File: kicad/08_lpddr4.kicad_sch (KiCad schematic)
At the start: 42 parts, among them U501 Ti135N484I3, U801 H9HCNNN8KUMLHR-NME

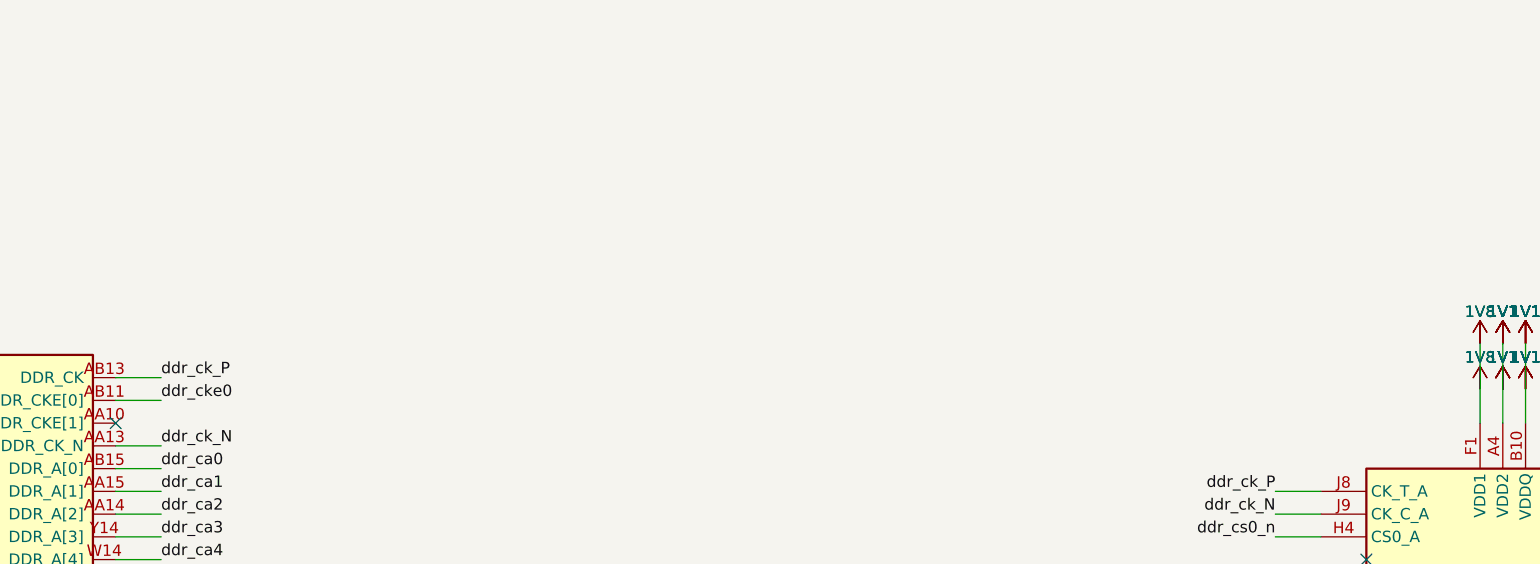
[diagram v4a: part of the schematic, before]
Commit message: CKE: 10 ohm series resistor R803 on B.Cu at the U501 CKE via
Sheet 08: U501 AB11 -> ddr_cke0_fpga -> R803 (10R 0402, C25077) -> ddr_cke0 -> U801 J4/P4; lpddr_ca netclass
pattern includes cke0_fpga. CKE has no ODT; at max corner / 3200 Mbps it peaked 16 mV over the overshoot limit,
with the resistor 179 mV under it (sim/lpddr4_si/results/routed_corners.md). Board: R803 placed on B.Cu on the
CKE via (user), CKE rerouted to it.

Co-Authored-By: Claude Opus 5.5 <noreply@anthropic.com>
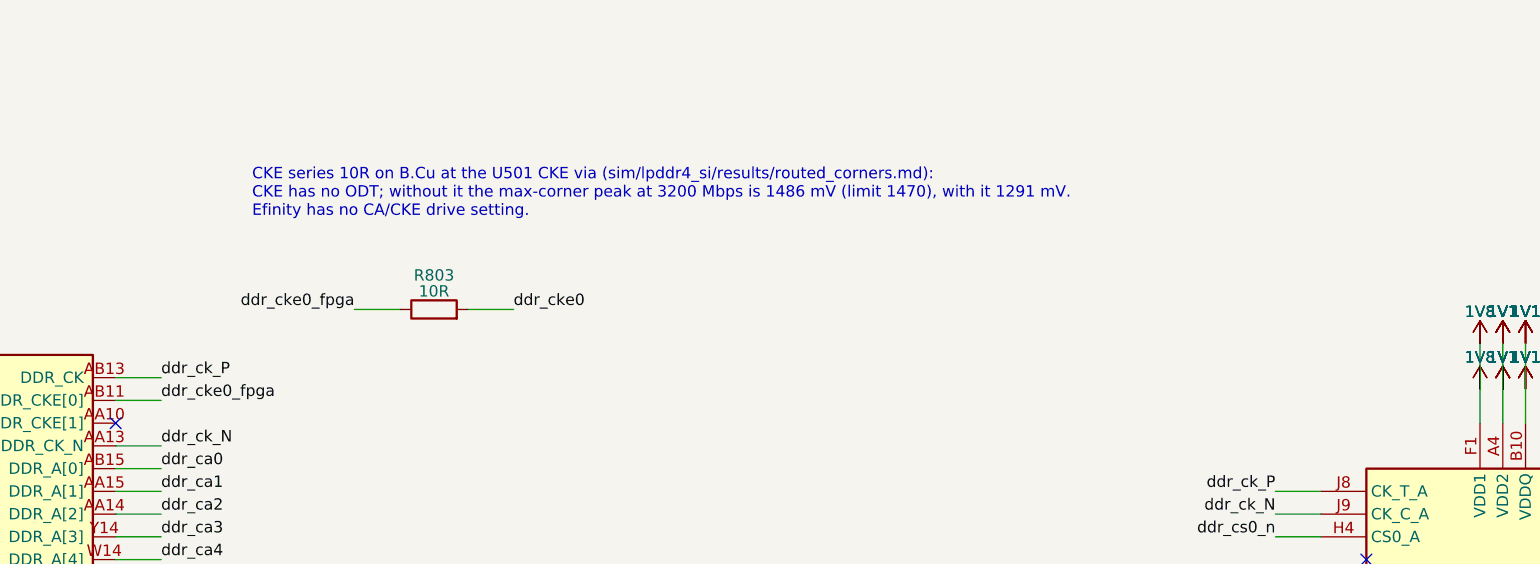
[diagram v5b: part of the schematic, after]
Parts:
- added R803: 10R, Resistor_SMD:R_0402_1005Metric, symbol ti135_card:R
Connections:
- net ddr_cke0: now also R803.2; no longer U501.AB11 (DDR_CKE[0])
- new net ddr_cke0_fpga: R803.1, U501.AB11 (DDR_CKE[0])
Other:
- note added: "CKE series 10R on B.Cu at the U501 CKE via (sim/lpddr4_si/results/routed_corners.md): CKE has no ODT; without it the max-corner peak at 3200 Mbps is 1486 mV (limit 1470), with it 1291 mV. Efinity has no CA/CKE drive setting."
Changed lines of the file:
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@@
 		)
 	)
-	(label "ddr_cke0"
+	(label "ddr_cke0_fpga"
 		(at 116.84 86.36 0)
 		(effects
@@
 		)
 	)
+	(symbol
+		(lib_id "ti135_card:R")
+		(at 147.32 76.2 90)
+		(unit 1)
+		(exclude_from_sim no)
+		(in_bom yes)
+		(on_board yes)
+		(dnp no)
+		(property "Reference" "R803"
+			(at 147.32 72.39 270)
+			(effects
+				(font
+					(size 1.27 1.27)
+				)
+			)
+		)
+		(property "Value" "10R"
+			(at 147.32 74.17 270)
+			(effects
+				(font
+					(size 1.27 1.27)
+				)
+			)
+		)
+		(property "Footprint" "Resistor_SMD:R_0402_1005Metric"
+			(at 147.32 77.978 0)
+			(effects
+				(font
+					(size 1.27 1.27)
+				)
+				(hide yes)
+			)
+		)
+		(property "Datasheet" ""
+			(at 147.32 76.2 0)
+			(effects
+				(font
+					(size 1.27 1.27)
+				)
+				(hide yes)
+			)
+		)
+		(property "Description" "Resistor"
+			(at 147.32 76.2 0)
+			(effects
+				(font
+					(size 1.27 1.27)
+				)
+				(hide yes)
+			)
+		)
+		(property "LCSC" "C25077"
+			(at 147.32 76.2 0)
+			(effects
+				(font
+					(size 1.27 1.27)
+				)
+				(hide yes)
+			)
+		)
+		(pin "1"
+		)
+		(pin "2"
+		)
+		(instances
+			(project "ti135_card"
+				(path "/c384d3ae-6e7d-47ca-8f4d-7f9f77efe4b7/df7ad03a-4cdc-47f6-9423-5d0632e27d2b"
+					(reference "R803")
+					(unit 1)
+				)
+			)
+		)
+	)
+	(wire
+		(pts
+			(xy 143.51 76.2) (xy 138.43 76.2)
+		)
+		(stroke
+			(width 0)
+			(type default)
+		)
+	)
+	(label "ddr_cke0_fpga"
+		(at 138.43 76.2 180)
+		(effects
+			(font
+				(size 1.27 1.27)
+			)
+			(justify right bottom)
+		)
+	)
+	(wire
+		(pts
+			(xy 151.13 76.2) (xy 156.21 76.2)
+		)
+		(stroke
+			(width 0)
+			(type default)
+		)
+	)
+	(label "ddr_cke0"
+		(at 156.21 76.2 0)
+		(effects
+			(font
+				(size 1.27 1.27)
+			)
+			(justify left bottom)
+		)
+	)
+	(text "CKE series 10R on B.Cu at the U501 CKE via (sim/lpddr4_si/results/routed_corners.md):\nCKE has no ODT; without it the max-corner peak at 3200 Mbps is 1486 mV (limit 1470), with it 1291 mV.\nEfinity has no CA/CKE drive setting."
+		(exclude_from_sim no)
+		(at 127 66.04 0)
+		(effects
+			(font
+				(size 1.27 1.27)
+			)
+			(justify left bottom)
+		)
+	)
